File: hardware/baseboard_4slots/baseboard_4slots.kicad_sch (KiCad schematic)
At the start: 59 parts, among them J1 IO-Board_00, J10 Conn_01x04_Male, J11 Conn_01x04_Male, J12 Conn_01x04_Male, J13 Conn_01x04_Male, J14 Conn_01x04_Male, J2 IO-Board_01, J3 IO-Board_10, J4 IO-Board_11, J5 USB_B_Micro, J6 Conn_01x05: Adafruit 1833, J7 Screw_Terminal_01x04, J8 Conn_02x02_Odd_Even, J9 Conn_02x02_Odd_Even, U1 NRF24L01_Breakout, U2 Pico

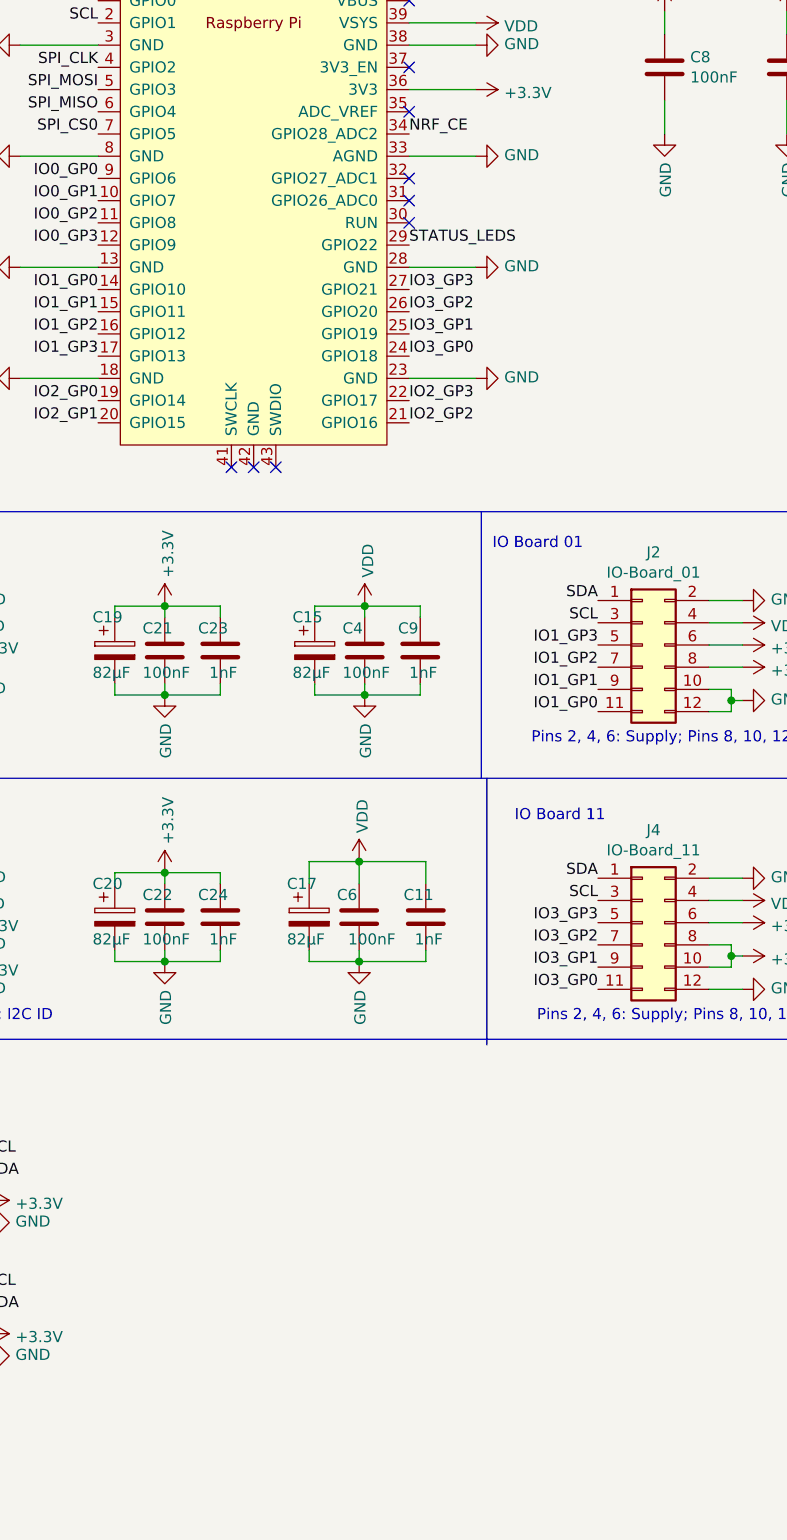
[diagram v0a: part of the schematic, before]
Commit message: Baseboard: Add W5500 Mini (WIZ850io) module. Needs verification
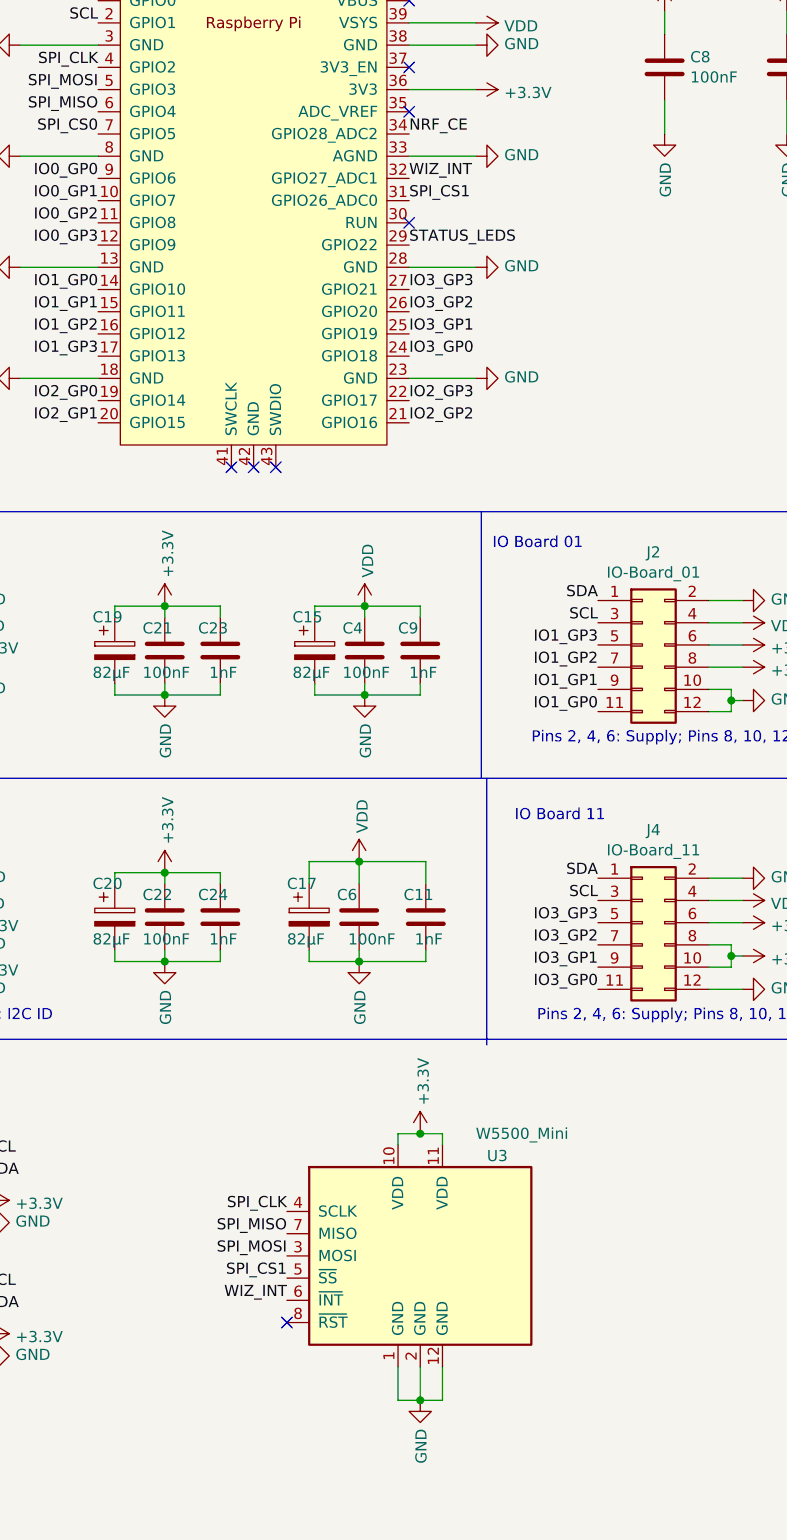
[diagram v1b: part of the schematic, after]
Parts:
- added U3: W5500_Mini, W5500_Mini:W5500_Mini, symbol W5500_Mini:W5500_Mini
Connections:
- net +3.3V: now also U3.10 (VDD), U3.11 (VDD)
- net GND: now also U3.1 (GND), U3.12 (GND), U3.2 (GND)
- net SPI_CLK: now also U3.4 (SCLK)
- net SPI_MISO: now also U3.7 (MISO)
- net SPI_MOSI: now also U3.3 (MOSI)
- net SPI_CS1: now reaches U2.31 (GPIO26_ADC0)
- net SPI_CS1: now also U3.5 (~{SS})
- net WIZ_INT: now reaches U2.32 (GPIO27_ADC1)
- net WIZ_INT: now also U3.6 (~{INT})
- no-connect marks 17 -> 16
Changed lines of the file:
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@@
   (junction (at 255.27 121.92) (diameter 0) (color 0 0 0 0)
   )
+  (junction (at 158.75 184.15) (diameter 0) (color 0 0 0 0)
+  )
   (junction (at 194.31 104.14) (diameter 0) (color 0 0 0 0)
   )
@@
   (junction (at 228.6 93.345) (diameter 0) (color 0 0 0 0)
   )
+  (junction (at 158.75 153.67) (diameter 0) (color 0 0 0 0)
+  )
   (junction (at 62.23 184.15) (diameter 0) (color 0 0 0 0)
   )
@@
   (no_connect (at 137.16 77.47))
   (no_connect (at 237.49 53.34))
-  (no_connect (at 157.48 46.99))
   (no_connect (at 237.49 50.8))
   (no_connect (at 157.48 31.75))
-  (no_connect (at 157.48 44.45))
+  (no_connect (at 143.51 175.26))
   (no_connect (at 139.7 77.47))
   (wire (pts (xy 194.31 132.08) (xy 194.31 133.35))
@@
     (stroke (width 0) (type default) (color 0 0 0 0))
   )
+  (wire (pts (xy 156.21 153.67) (xy 158.75 153.67))
+    (stroke (width 0) (type default) (color 0 0 0 0))
+  )
   (wire (pts (xy 100.33 97.79) (xy 104.14 97.79))
     (stroke (width 0) (type default) (color 0 0 0 0))
@@
     (stroke (width 0) (type default) (color 0 0 0 0))
   )
+  (wire (pts (xy 161.29 153.67) (xy 158.75 153.67))
+    (stroke (width 0) (type default) (color 0 0 0 0))
+  )
   (polyline (pts (xy 68.58 198.12) (xy 12.7 198.12))
     (stroke (width 0) (type default) (color 0 0 0 0))
@@
     (stroke (width 0) (type default) (color 0 0 0 0))
   )
+  (wire (pts (xy 156.21 180.34) (xy 156.21 184.15))
+    (stroke (width 0) (type default) (color 0 0 0 0))
+  )
   (polyline (pts (xy 68.58 113.03) (xy 281.94 113.03))
     (stroke (width 0) (type default) (color 0 0 0 0))
@@
     (stroke (width 0) (type default) (color 0 0 0 0))
   )
+  (wire (pts (xy 156.21 154.94) (xy 156.21 153.67))
+    (stroke (width 0) (type default) (color 0 0 0 0))
+  )
   (wire (pts (xy 104.14 137.16) (xy 100.33 137.16))
     (stroke (width 0) (type default) (color 0 0 0 0))
@@
     (stroke (width 0) (type default) (color 0 0 0 0))
   )
+  (wire (pts (xy 161.29 184.15) (xy 158.75 184.15))
+    (stroke (width 0) (type default) (color 0 0 0 0))
+  )
   (wire (pts (xy 255.27 124.46) (xy 255.27 121.92))
     (stroke (width 0) (type default) (color 0 0 0 0))
@@
     (stroke (width 0) (type default) (color 0 0 0 0))
   )
+  (wire (pts (xy 158.75 180.34) (xy 158.75 184.15))
+    (stroke (width 0) (type default) (color 0 0 0 0))
+  )
   (wire (pts (xy 255.27 104.775) (xy 255.27 103.505))
     (stroke (width 0) (type default) (color 0 0 0 0))
@@
     (stroke (width 0) (type default) (color 0 0 0 0))
   )
+  (wire (pts (xy 161.29 180.34) (xy 161.29 184.15))
+    (stroke (width 0) (type default) (color 0 0 0 0))
+  )
   (wire (pts (xy 249.555 104.775) (xy 255.27 104.775))
     (stroke (width 0) (type default) (color 0 0 0 0))
@@
     (stroke (width 0) (type default) (color 0 0 0 0))
   )
+  (wire (pts (xy 156.21 184.15) (xy 158.75 184.15))
+    (stroke (width 0) (type default) (color 0 0 0 0))
+  )
   (polyline (pts (xy 214.63 12.7) (xy 214.63 82.55))
     (stroke (width 0) (type default) (color 0 0 0 0))
@@
     (stroke (width 0) (type default) (color 0 0 0 0))
   )
+  (wire (pts (xy 161.29 154.94) (xy 161.29 153.67))
+    (stroke (width 0) (type default) (color 0 0 0 0))
+  )
   (wire (pts (xy 106.68 171.45) (xy 109.22 171.45))
     (stroke (width 0) (type default) (color 0 0 0 0))
@@
     (effects (font (size 1.27 1.27)) (justify right bottom))
   )
+  (label "WIZ_INT" (at 157.48 44.45 0)
+    (effects (font (size 1.27 1.27)) (justify left bottom))
+  )
   (label "SCL" (at 179.07 127 180)
     (effects (font (size 1.27 1.27)) (justify right bottom))
@@
     (effects (font (size 1.27 1.27)) (justify right bottom))
   )
+  (label "WIZ_INT" (at 143.51 172.72 180)
+    (effects (font (size 1.27 1.27)) (justify right bottom))
+  )
   (label "SDA" (at 87.63 92.71 180)
     (effects (font (size 1.27 1.27)) (justify right bottom))
@@
     (effects (font (size 1.27 1.27)) (justify left bottom))
   )
+  (label "SPI_CS1" (at 143.51 170.18 180)
+    (effects (font (size 1.27 1.27)) (justify right bottom))
+  )
   (label "IO1_GP2" (at 179.07 100.33 180)
     (effects (font (size 1.27 1.27)) (justify right bottom))
@@
     (effects (font (size 1.27 1.27)) (justify right bottom))
   )
+  (label "SPI_MISO" (at 143.51 165.1 180)
+    (effects (font (size 1.27 1.27)) (justify right bottom))
+  )
   (label "SCL" (at 87.63 156.21 0)
     (effects (font (size 1.27 1.27)) (justify left bottom))
@@
     (effects (font (size 1.27 1.27)) (justify right bottom))
   )
+  (label "SPI_CS1" (at 157.48 46.99 0)
+    (effects (font (size 1.27 1.27)) (justify left bottom))
+  )
+  (label "SPI_CLK" (at 143.51 162.56 180)
+    (effects (font (size 1.27 1.27)) (justify right bottom))
+  )
   (label "SDA" (at 87.63 124.46 180)
     (effects (font (size 1.27 1.27)) (justify right bottom))
@@
     (effects (font (size 1.27 1.27)) (justify left bottom))
   )
+  (label "SPI_MOSI" (at 143.51 167.64 180)
+    (effects (font (size 1.27 1.27)) (justify right bottom))
+  )
   (label "IO2_GP3" (at 157.48 69.85 0)
     (effects (font (size 1.27 1.27)) (justify left bottom))
@@
     (pin "1")
   )
+  (symbol (lib_id "power:+3.3V") (at 158.75 153.67 0) (unit 1)
+    (in_bom yes) (on_board yes)
+    (property "Reference" "#PWR062" (id 0) (at 158.75 157.48 0)
+      (effects (font (size 1.27 1.27)) hide)
+    )
+    (property "Value" "+3.3V" (id 1) (at 159.131 150.4188 90)
+      (effects (font (size 1.27 1.27)) (justify left))
+    )
+    (property "Footprint" "" (id 2) (at 158.75 153.67 0)
+      (effects (font (size 1.27 1.27)) hide)
+    )
+    (property "Datasheet" "" (id 3) (at 158.75 153.67 0)
+      (effects (font (size 1.27 1.27)) hide)
+    )
+    (pin "1")
+  )
   (symbol (lib_id "power:GND") (at 228.6 103.505 0) (unit 1)
     (in_bom yes) (on_board yes)
@@
     (pin "1")
   )
+  (symbol (lib_id "W5500_Mini:W5500_Mini") (at 158.75 168.91 0) (unit 1)
+    (in_bom yes) (on_board yes)
+    (property "Reference" "U3" (id 0) (at 166.37 156.21 0)
+      (effects (font (size 1.27 1.27)) (justify left))
+    )
+    (property "Value" "W5500_Mini" (id 1) (at 165.1 153.67 0)
+      (effects (font (size 1.27 1.27)) (justify left))
+    )
+    (property "Footprint" "W5500_Mini:W5500_Mini" (id 2) (at 170.18 170.18 0)
+      (effects (font (size 1.27 1.27)) hide)
+    )
+    (property "Datasheet" "" (id 3) (at 158.75 168.91 0)
+      (effects (font (size 1.27 1.27)) hide)
+    )
+    (pin "1")
+    (pin "10")
+    (pin "11")
+    (pin "12")
+    (pin "2")
+    (pin "3")
+    (pin "4")
+    (pin "5")
+    (pin "6")
+    (pin "7")
+    (pin "8")
+    (pin "9")
+  )
   (symbol (lib_id "Device:C_Polarized") (at 146.05 128.905 0) (unit 1)
     (in_bom yes) (on_board yes)
@@
     (pin "1")
   )
+  (symbol (lib_id "power:GND") (at 158.75 184.15 0) (unit 1)
+    (in_bom yes) (on_board yes)
+    (property "Reference" "#PWR063" (id 0) (at 158.75 190.5 0)
+      (effects (font (size 1.27 1.27)) hide)
+    )
+    (property "Value" "GND" (id 1) (at 158.877 187.4012 90)
+      (effects (font (size 1.27 1.27)) (justify right))
+    )
+    (property "Footprint" "" (id 2) (at 158.75 184.15 0)
+      (effects (font (size 1.27 1.27)) hide)
+    )
+    (property "Datasheet" "" (id 3) (at 158.75 184.15 0)
+      (effects (font (size 1.27 1.27)) hide)
+    )
+    (pin "1")
+  )
   (symbol (lib_id "Device:C_Polarized") (at 222.885 127.635 0) (unit 1)
     (in_bom yes) (on_board yes)
@@
       (reference "#PWR061") (unit 1) (value "GND") (footprint "")
     )
+    (path "/187fb50d-a16a-4c94-9a98-713e250d2593"
+      (reference "#PWR062") (unit 1) (value "+3.3V") (footprint "")
+    )
+    (path "/bcb6241b-568e-468d-90be-e2f8e5b96935"
+      (reference "#PWR063") (unit 1) (value "GND") (footprint "")
+    )
     (path "/00000000-0000-0000-0000-000060611674"
       (reference "#PWR0101") (unit 1) (value "GND") (footprint "")
@@
       (reference "U2") (unit 1) (value "Pico") (footprint "MCU_RaspberryPi_and_Boards:RPi_Pico_SMD_TH")
     )
+    (path "/4626df37-d76f-45a7-afd7-a90c89a1d1ad"
+      (reference "U3") (unit 1) (value "W5500_Mini") (footprint "W5500_Mini:W5500_Mini")
+    )
   )
